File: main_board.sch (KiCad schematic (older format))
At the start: 17 parts, among them U2 QM_XC7A35T_DDR3

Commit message: Add Max9850 to handle audio.
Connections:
- net labels added: MAX_I2S0, MAX_LRCLK, MAX_SCLK
- net labels removed: AUDIO_LEFT, AUDIO_RIGHT
- no-connect marks 26 -> 25
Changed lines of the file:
@@
 Text GLabel 3600 2350 2    50   Input ~ 0
 3V3
-Text GLabel 8350 5050 0    50   Input ~ 0
-AUDIO_LEFT
-Text GLabel 8350 5150 0    50   Input ~ 0
-AUDIO_RIGHT
 Text GLabel 8350 2250 0    50   Input ~ 0
 GND
@@
 NoConn ~ 9950 3450
 NoConn ~ 9950 3550
-NoConn ~ 8350 4750
-NoConn ~ 8350 4650
 NoConn ~ 8350 4550
 NoConn ~ 1850 4050
@@
 Text Label 8350 4950 2    50   ~ 0
 LED7
+Text GLabel 8350 5150 0    50   Input ~ 0
+MAX_LRCLK
+Text GLabel 8350 5050 0    50   Input ~ 0
+MAX_SCLK
+Text GLabel 8350 4750 0    50   Input ~ 0
+MAX_I2S0
+NoConn ~ 8350 4650
 $EndSCHEMATC

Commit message: Change order of the VSPI to FPGA to make sure the clock pin connects to an FPGA clock capable pin.
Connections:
- no-connect marks 25 -> 24
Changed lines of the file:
@@
 Text GLabel 8350 4450 0    50   Input ~ 0
 ADV_LRCLK
-Text GLabel 8350 4550 0    50   Input ~ 0
+Text GLabel 1850 3250 0    50   Input ~ 0
 ADV_INT
 NoConn ~ 9950 3350
@@
 Text GLabel 3450 4950 2    50   Input ~ 0
 EXP_35
+Text GLabel 1850 3050 0    50   Input ~ 0
+ESP_VSPI_CLK
 Text GLabel 1850 2850 0    50   Input ~ 0
-ESP_VSPI_CLK
+ESP_VSPI_MISO
 Text GLabel 1850 2950 0    50   Input ~ 0
-ESP_VSPI_MISO
-Text GLabel 1850 3050 0    50   Input ~ 0
 ESP_VSPI_MOSI
 Text GLabel 1850 3150 0    50   Input ~ 0
@@
 NoConn ~ 3450 5050
 NoConn ~ 3450 5150
-NoConn ~ 1850 3250
 NoConn ~ 8350 4150
 NoConn ~ 8350 4250

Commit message: Add PS/2 Mouse connector to the board, USB has too much overhead.
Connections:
- net labels added: ESP_INT, PS2_CLK2, PS2_DAT2
- no-connect marks 24 -> 21
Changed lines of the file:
@@
 Text GLabel 8350 4450 0    50   Input ~ 0
 ADV_LRCLK
-Text GLabel 1850 3250 0    50   Input ~ 0
+Text GLabel 1850 3450 0    50   Input ~ 0
 ADV_INT
 NoConn ~ 9950 3350
 NoConn ~ 9950 3450
 NoConn ~ 9950 3550
-NoConn ~ 8350 4550
-NoConn ~ 1850 4050
 NoConn ~ 1850 3950
 NoConn ~ 1850 3850
@@
 Text GLabel 1850 3050 0    50   Input ~ 0
 ESP_VSPI_CLK
-Text GLabel 1850 2850 0    50   Input ~ 0
+Text GLabel 1850 3150 0    50   Input ~ 0
 ESP_VSPI_MISO
-Text GLabel 1850 2950 0    50   Input ~ 0
+Text GLabel 1850 3250 0    50   Input ~ 0
 ESP_VSPI_MOSI
-Text GLabel 1850 3150 0    50   Input ~ 0
+Text GLabel 1850 3350 0    50   Input ~ 0
 ESP_VSPI_CS
 Text GLabel 8350 2750 0    50   Input ~ 0
@@
 NoConn ~ 1850 3650
 NoConn ~ 1850 3550
-NoConn ~ 1850 3450
-NoConn ~ 1850 3350
 NoConn ~ 1850 5050
 NoConn ~ 1850 5150
@@
 Text GLabel 8350 4750 0    50   Input ~ 0
 MAX_I2S0
-NoConn ~ 8350 4650
+NoConn ~ 1850 2850
+NoConn ~ 1850 2950
+Text GLabel 1850 4050 0    50   Input ~ 0
+ESP_INT
+Text GLabel 8350 4550 0    50   Input ~ 0
+PS2_CLK2
+Text GLabel 8350 4650 0    50   Input ~ 0
+PS2_DAT2
 $EndSCHEMATC

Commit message: First checkin of SDRAM Open AARS board.
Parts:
- removed D31: 7, LED_SMD:LED_0603_1608Metric, symbol Device:LED
- removed D32: 6, LED_SMD:LED_0603_1608Metric, symbol Device:LED
- removed D5: 5, LED_SMD:LED_0603_1608Metric, symbol Device:LED
- removed D6: 4, LED_SMD:LED_0603_1608Metric, symbol Device:LED
- removed R48, R49, R63, R64: 1k, Resistor_SMD:R_0603_1608Metric, symbol Device:R
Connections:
- net labels added: FLP_LPI_INTA, FLP_SPI_CS, FLP_SPI_INTB, FLP_SPI_MISO, FLP_SPI_MOSI, FLP_SPI_SCK, JS_CS, JS_INTA, JS_INTB, JS_MISO, JS_MOSI, JS_SCK, SDRAM_A0, SDRAM_A1, SDRAM_A10, SDRAM_A11, SDRAM_A2, SDRAM_A3, SDRAM_A4, SDRAM_A5, SDRAM_A6, SDRAM_A7, SDRAM_A8, SDRAM_A9, SDRAM_BA0, SDRAM_BA1, SDRAM_CAS, SDRAM_CKE, SDRAM_CLK, SDRAM_CS, SDRAM_D0, SDRAM_D1, SDRAM_D2, SDRAM_D3, SDRAM_D4, SDRAM_D5, SDRAM_D6, SDRAM_D7, SDRAM_DQ10, SDRAM_DQ11, SDRAM_DQ12, SDRAM_DQ13, SDRAM_DQ14, SDRAM_DQ15, SDRAM_DQ8, SDRAM_DQ9, SDRAM_DQMH, SDRAM_DQML, SDRAM_RAS, SDRAM_WE
- net labels removed: EXP_02, EXP_04, EXP_08, EXP_10, EXP_12, EXP_16, EXP_18, EXP_20, EXP_22, EXP_24, EXP_26, EXP_28, EXP_30, EXP_32, EXP_34, EXP_35, JS1_1, JS1_2, JS1_3, JS1_4, JS1_5, JS1_6, JS1_7, JS1_9, JS2_1, JS2_2, JS2_3, JS2_4, JS2_5, JS2_6, JS2_7, JS2_9, LED4, LED5, LED6, LED7
- wire segments 40 -> 23
- no-connect marks 21 -> 0

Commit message: Implemented the Floppy interface, fixed 12V power up issue with the board.
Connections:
- net labels added: EXP_CHNG, EXP_DIR, EXP_DKRD, EXP_DKWDB, EXP_DKWEB, EXP_INDEX, EXP_RDY, EXP_SEL0, EXP_SEL1, EXP_SIDE, EXP_STEP, EXP_TRK0
- net labels removed: FLP_LPI_INTA, FLP_SPI_CS, FLP_SPI_INTB, FLP_SPI_MISO, FLP_SPI_MOSI, FLP_SPI_SCK
- wire segments 23 -> 22
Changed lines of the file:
@@
 VIN5V
-Wire Wire Line
-	1850 5250 1700 5250
 Wire Wire Line
 	1850 5350 1700 5350
@@
 Text GLabel 3450 3050 2    50   Input ~ 0
 ADV_G_5
-Text GLabel 1850 2950 0    50   Input ~ 0
+Text GLabel 1850 3050 0    50   Input ~ 0
 ADV_G_6
 Text GLabel 3450 2950 2    50   Input ~ 0
@@
 Text Label 2700 7100 3    50   ~ 0
 LED0
-Text Label 9950 4650 0    50   ~ 0
+Text Label 9950 4350 0    50   ~ 0
 LED0
 Text Label 9950 4750 0    50   ~ 0
@@
 Text GLabel 1850 3450 0    50   Input ~ 0
 ADV_INT
-Text GLabel 1850 3050 0    50   Input ~ 0
+Text GLabel 1850 2950 0    50   Input ~ 0
 ESP_VSPI_CLK
 Text GLabel 1850 3150 0    50   Input ~ 0
@@
 Text GLabel 8350 4650 0    50   Input ~ 0
 JS_INTB
+Text GLabel 9950 4550 2    50   Input ~ 0
+JS_INTA
 Text GLabel 8350 4550 0    50   Input ~ 0
-JS_INTA
-Text GLabel 9950 4550 2    50   Input ~ 0
 JS_CS
+Text GLabel 9950 4450 2    50   Input ~ 0
+JS_MISO
 Text GLabel 8350 4450 0    50   Input ~ 0
-JS_MISO
-Text GLabel 9950 4450 2    50   Input ~ 0
 JS_MOSI
-Text GLabel 9950 4350 2    50   Input ~ 0
+Text GLabel 9950 4650 2    50   Input ~ 0
 JS_SCK
+Text GLabel 1850 4650 0    50   Input ~ 0
+EXP_SEL0
+Text GLabel 3450 4650 2    50   Input ~ 0
+EXP_SEL1
+Text GLabel 1850 4750 0    50   Input ~ 0
+EXP_DIR
+Text GLabel 3450 4750 2    50   Input ~ 0
+EXP_STEP
+Text GLabel 1850 4850 0    50   Input ~ 0
+EXP_CHNG
+Text GLabel 3450 4850 2    50   Input ~ 0
+EXP_INDEX
+Text GLabel 1850 4950 0    50   Input ~ 0
+EXP_RDY
+Text GLabel 3450 4950 2    50   Input ~ 0
+EXP_DKRD
+Text GLabel 3450 5050 2    50   Input ~ 0
+EXP_DKWDB
 Text GLabel 1850 5150 0    50   Input ~ 0
-FLP_SPI_MOSI
-Text GLabel 3450 5050 2    50   Input ~ 0
-FLP_SPI_SCK
+EXP_DKWEB
+Text GLabel 1850 5050 0    50   Input ~ 0
+EXP_TRK0
 Text GLabel 3450 5150 2    50   Input ~ 0
-FLP_SPI_MISO
-Text GLabel 1850 5050 0    50   Input ~ 0
-FLP_SPI_CS
-Text GLabel 3450 4950 2    50   Input ~ 0
-FLP_SPI_INTB
-Text GLabel 1850 4950 0    50   Input ~ 0
-FLP_LPI_INTA
+EXP_SIDE
 $EndSCHEMATC

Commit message: Version that was sent to JLCPCB 20200716.
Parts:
- added C67: 22UF, Capacitor_SMD:CP_Elec_5x5.4, symbol Device:CP
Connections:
- net labels added: EXP_MTRON
- wire segments 22 -> 26
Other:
- note added: "Decoupling Cap\n"
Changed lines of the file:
@@
 Text GLabel 3450 5150 2    50   Input ~ 0
 EXP_SIDE
+Text GLabel 9950 4250 2    50   Input ~ 0
+EXP_MTRON
+$Comp
+L Device:CP C?
+U 1 1 5FD13792
+P 3875 6600
+AR Path="/5DE41876/5FD13792" Ref="C?"  Part="1"
+AR Path="/5D7064D1/5FD13792" Ref="C67"  Part="1"
+F 0 "C67" H 3993 6646 50  0000 L CNN
+F 1 "22UF" H 3993 6555 50  0000 L CNN
+F 2 "Capacitor_SMD:CP_Elec_5x5.4" H 3913 6450 50  0001 C CNN
+F 3 "~" H 3875 6600 50  0001 C CNN
+	1    3875 6600
+	1    0    0    -1
+$EndComp
+Wire Wire Line
+	3725 6350 3875 6350
+Wire Wire Line
+	3875 6350 3875 6450
+Wire Wire Line
+	3875 6750 3875 6875
+Wire Wire Line
+	3875 6875 3725 6875
+Text GLabel 3725 6350 0    50   Input ~ 0
+VIN5V
+Text GLabel 3725 6875 0    50   Input ~ 0
+GND
+Text Notes 3475 6275 0    50   ~ 0
+Decoupling Cap\n
 $EndSCHEMATC

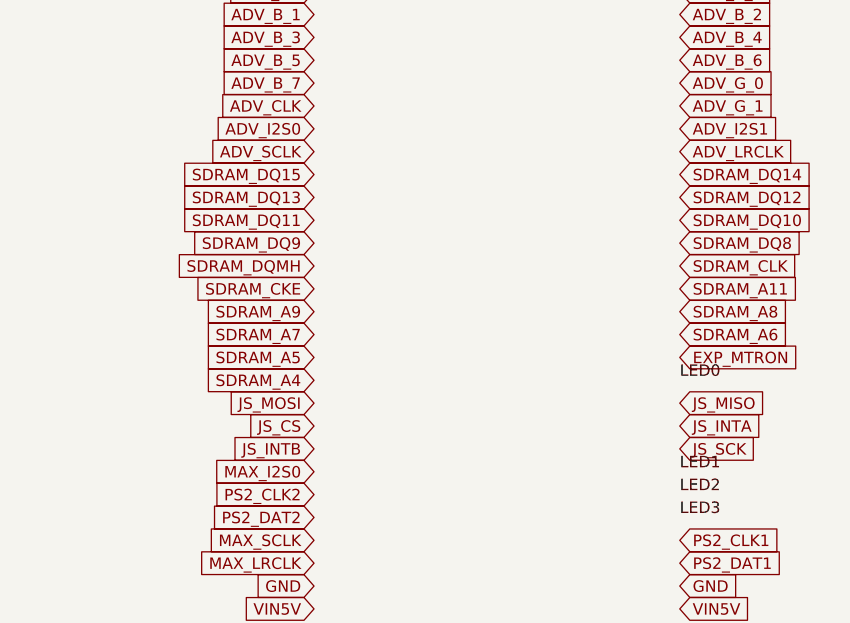
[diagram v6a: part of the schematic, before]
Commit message: Fixed SDRAM_A12 missing route, disconnected JS_INT_B.
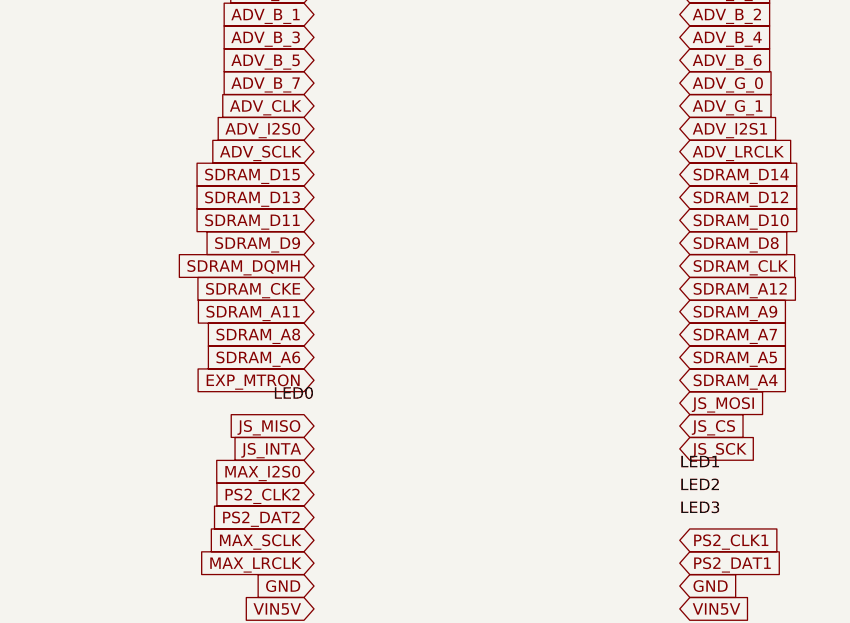
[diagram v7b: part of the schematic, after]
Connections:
- net labels added: SDRAM_A12, SDRAM_D10, SDRAM_D11, SDRAM_D12, SDRAM_D13, SDRAM_D14, SDRAM_D15, SDRAM_D8, SDRAM_D9
- net labels removed: JS_INTB, SDRAM_DQ10, SDRAM_DQ11, SDRAM_DQ12, SDRAM_DQ13, SDRAM_DQ14, SDRAM_DQ15, SDRAM_DQ8, SDRAM_DQ9
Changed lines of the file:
@@
 Text Label 2700 7100 3    50   ~ 0
 LED0
-Text Label 9950 4350 0    50   ~ 0
+Text Label 8350 4450 2    50   ~ 0
 LED0
 Text Label 9950 4750 0    50   ~ 0
@@
 Text GLabel 8350 4950 0    50   Input ~ 0
 PS2_DAT2
-$Comp
-L QM_XC7A35T_DDR3:QM_XC7A35T_DDR3 U2
-U 1 1 5D70654A
-P 5950 3750
-AR Path="/5D70654A" Ref="U2"  Part="1"
-AR Path="/5D7064D1/5D70654A" Ref="U2"  Part="1"
-F 0 "U2" H 5919 5605 50  0000 C CNN
-F 1 "QM_XC7A35T_DDR3" H 5919 5514 50  0000 C CNN
-F 2 "QM_XC7A35T_DDR3:QM_XC7A35T_DDR3_Daughterboard" H 5919 5423 50  0000 C CNN
-F 3 "" H 2650 2300 50  0001 C CNN
-	1    5950 3750
-	1    0    0    -1
-$EndComp
 Text GLabel 3450 3650 2    50   Input ~ 0
 SDRAM_D0
@@
 SDRAM_A3
 Text GLabel 8350 3450 0    50   Input ~ 0
-SDRAM_DQ15
+SDRAM_D15
 Text GLabel 9950 3450 2    50   Input ~ 0
-SDRAM_DQ14
+SDRAM_D14
 Text GLabel 8350 3550 0    50   Input ~ 0
-SDRAM_DQ13
+SDRAM_D13
 Text GLabel 9950 3550 2    50   Input ~ 0
-SDRAM_DQ12
+SDRAM_D12
 Text GLabel 8350 3650 0    50   Input ~ 0
-SDRAM_DQ11
+SDRAM_D11
 Text GLabel 9950 3650 2    50   Input ~ 0
-SDRAM_DQ10
+SDRAM_D10
 Text GLabel 8350 3750 0    50   Input ~ 0
-SDRAM_DQ9
+SDRAM_D9
 Text GLabel 9950 3750 2    50   Input ~ 0
-SDRAM_DQ8
+SDRAM_D8
 Text GLabel 8350 3850 0    50   Input ~ 0
 SDRAM_DQMH
@@
 Text GLabel 8350 3950 0    50   Input ~ 0
 SDRAM_CKE
-Text GLabel 9950 3950 2    50   Input ~ 0
-SDRAM_A11
-Text GLabel 8350 4050 0    50   Input ~ 0
-SDRAM_A9
-Text GLabel 9950 4050 2    50   Input ~ 0
-SDRAM_A8
-Text GLabel 8350 4150 0    50   Input ~ 0
-SDRAM_A7
-Text GLabel 9950 4150 2    50   Input ~ 0
-SDRAM_A6
-Text GLabel 8350 4250 0    50   Input ~ 0
-SDRAM_A5
-Text GLabel 8350 4350 0    50   Input ~ 0
-SDRAM_A4
 Text GLabel 3450 4250 2    50   Input ~ 0
 SDRAM_CS
@@
 SDRAM_BA0
 Text GLabel 8350 4650 0    50   Input ~ 0
-JS_INTB
-Text GLabel 9950 4550 2    50   Input ~ 0
 JS_INTA
 Text GLabel 8350 4550 0    50   Input ~ 0
-JS_CS
-Text GLabel 9950 4450 2    50   Input ~ 0
 JS_MISO
-Text GLabel 8350 4450 0    50   Input ~ 0
-JS_MOSI
 Text GLabel 9950 4650 2    50   Input ~ 0
 JS_SCK
@@
 Text GLabel 3450 5150 2    50   Input ~ 0
 EXP_SIDE
-Text GLabel 9950 4250 2    50   Input ~ 0
-EXP_MTRON
 $Comp
 L Device:CP C?
@@
 Text Notes 3475 6275 0    50   ~ 0
 Decoupling Cap\n
+Text GLabel 8350 4350 0    50   Input ~ 0
+EXP_MTRON
+Text GLabel 8350 4250 0    50   Input ~ 0
+SDRAM_A6
+Text GLabel 8350 4150 0    50   Input ~ 0
+SDRAM_A8
+Text GLabel 8350 4050 0    50   Input ~ 0
+SDRAM_A11
+Text GLabel 9950 4450 2    50   Input ~ 0
+JS_MOSI
+Text GLabel 9950 4550 2    50   Input ~ 0
+JS_CS
+Text GLabel 9950 4350 2    50   Input ~ 0
+SDRAM_A4
+Text GLabel 9950 4250 2    50   Input ~ 0
+SDRAM_A5
+Text GLabel 9950 4150 2    50   Input ~ 0
+SDRAM_A7
+Text GLabel 9950 4050 2    50   Input ~ 0
+SDRAM_A9
+$Comp
+L QM_XC7A35T_DDR3:QM_XC7A35T_DDR3 U2
+U 1 1 5D70654A
+P 5950 3750
+AR Path="/5D70654A" Ref="U2"  Part="1"
+AR Path="/5D7064D1/5D70654A" Ref="U2"  Part="1"
+F 0 "U2" H 5919 5605 50  0000 C CNN
+F 1 "QM_XC7A35T_DDR3" H 5919 5514 50  0000 C CNN
+F 2 "QM_XC7A35T_DDR3:QM_XC7A35T_DDR3_Daughterboard" H 5919 5423 50  0000 C CNN
+F 3 "" H 2650 2300 50  0001 C CNN
+	1    5950 3750
+	1    0    0    -1
+$EndComp
+Text GLabel 9950 3950 2    50   Input ~ 0
+SDRAM_A12
 $EndSCHEMATC

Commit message: Fixed I2C pullup resistors.
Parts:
- C67: value 22UF -> 22uF
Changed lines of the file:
@@
 AR Path="/5D7064D1/5FD13792" Ref="C67"  Part="1"
 F 0 "C67" H 3993 6646 50  0000 L CNN
-F 1 "22UF" H 3993 6555 50  0000 L CNN
+F 1 "22uF" H 3993 6555 50  0000 L CNN
 F 2 "Capacitor_SMD:CP_Elec_5x5.4" H 3913 6450 50  0001 C CNN
 F 3 "~" H 3875 6600 50  0001 C CNN
